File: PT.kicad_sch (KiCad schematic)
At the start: 4 parts

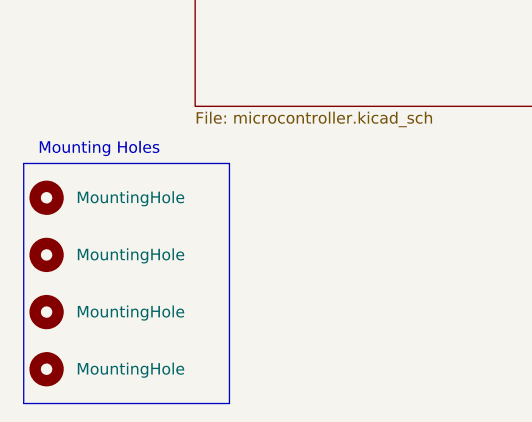
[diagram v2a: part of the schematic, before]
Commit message: Swap to STM32H563RIV6, and add split +3.3V and +3.3VA
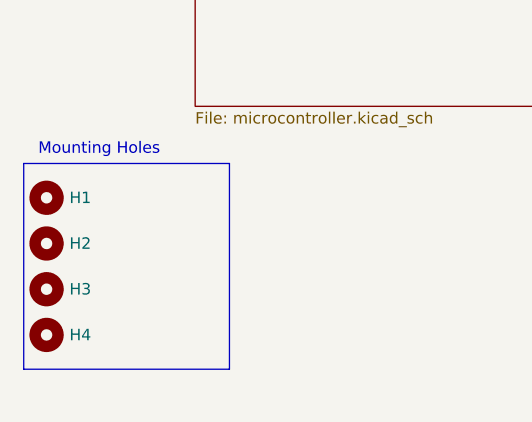
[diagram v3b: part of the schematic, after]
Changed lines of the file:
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@@
 	(rectangle
 		(start 20.32 172.72)
-		(end 43.18 199.39)
+		(end 43.18 195.58)
 		(stroke
 			(width 0)
@@
 	(symbol
 		(lib_id "Mechanical:MountingHole")
-		(at 22.86 189.23 0)
+		(at 22.86 176.53 0)
 		(unit 1)
 		(body_style 1)
@@
 		(in_pos_files yes)
 		(dnp no)
-		(property "Reference" "H3"
-			(at 25.4 187.9599 0)
-			(hide yes)
+		(property "Reference" "H1"
+			(at 25.4 176.53 0)
 			(show_name no)
 			(do_not_autoplace no)
@@
 		)
 		(property "Value" "MountingHole"
-			(at 26.162 189.23 0)
+			(at 26.162 176.53 0)
+			(hide yes)
 			(show_name no)
 			(do_not_autoplace no)
@@
 		)
 		(property "Footprint" "MountingHole:MountingHole_3.2mm_M3"
-			(at 22.86 189.23 0)
+			(at 22.86 176.53 0)
 			(hide yes)
 			(show_name no)
@@
 		)
 		(property "Datasheet" ""
-			(at 22.86 189.23 0)
+			(at 22.86 176.53 0)
 			(hide yes)
 			(show_name no)
@@
 		)
 		(property "Description" "Mounting Hole without connection"
-			(at 22.86 189.23 0)
+			(at 22.86 176.53 0)
 			(hide yes)
 			(show_name no)
@@
 			(project "PT"
 				(path "/0eb5ae8a-84ea-4b7e-bec4-bb4e0217d666"
-					(reference "H3")
+					(reference "H1")
 					(unit 1)
 				)
@@
 	(symbol
 		(lib_id "Mechanical:MountingHole")
-		(at 22.86 176.53 0)
+		(at 22.86 186.69 0)
 		(unit 1)
 		(body_style 1)
@@
 		(in_pos_files yes)
 		(dnp no)
-		(property "Reference" "H1"
-			(at 25.4 175.2599 0)
-			(hide yes)
+		(property "Reference" "H3"
+			(at 25.4 186.69 0)
 			(show_name no)
 			(do_not_autoplace no)
@@
 		)
 		(property "Value" "MountingHole"
-			(at 26.162 176.53 0)
+			(at 26.162 186.69 0)
+			(hide yes)
 			(show_name no)
 			(do_not_autoplace no)
@@
 		)
 		(property "Footprint" "MountingHole:MountingHole_3.2mm_M3"
-			(at 22.86 176.53 0)
+			(at 22.86 186.69 0)
 			(hide yes)
 			(show_name no)
@@
 		)
 		(property "Datasheet" ""
-			(at 22.86 176.53 0)
+			(at 22.86 186.69 0)
 			(hide yes)
 			(show_name no)
@@
 		)
 		(property "Description" "Mounting Hole without connection"
-			(at 22.86 176.53 0)
+			(at 22.86 186.69 0)
 			(hide yes)
 			(show_name no)
@@
 			(project "PT"
 				(path "/0eb5ae8a-84ea-4b7e-bec4-bb4e0217d666"
-					(reference "H1")
+					(reference "H3")
 					(unit 1)
 				)
@@
 	(symbol
 		(lib_id "Mechanical:MountingHole")
-		(at 22.86 182.88 0)
+		(at 22.86 191.77 0)
 		(unit 1)
 		(body_style 1)
@@
 		(in_pos_files yes)
 		(dnp no)
-		(property "Reference" "H2"
-			(at 25.4 181.6099 0)
-			(hide yes)
+		(property "Reference" "H4"
+			(at 25.4 191.77 0)
 			(show_name no)
 			(do_not_autoplace no)
@@
 		)
 		(property "Value" "MountingHole"
-			(at 26.162 182.88 0)
+			(at 26.162 191.77 0)
+			(hide yes)
 			(show_name no)
 			(do_not_autoplace no)
@@
 		)
 		(property "Footprint" "MountingHole:MountingHole_3.2mm_M3"
-			(at 22.86 182.88 0)
+			(at 22.86 191.77 0)
 			(hide yes)
 			(show_name no)
@@
 		)
 		(property "Datasheet" ""
-			(at 22.86 182.88 0)
+			(at 22.86 191.77 0)
 			(hide yes)
 			(show_name no)
@@
 		)
 		(property "Description" "Mounting Hole without connection"
-			(at 22.86 182.88 0)
+			(at 22.86 191.77 0)
 			(hide yes)
 			(show_name no)
@@
 			(project "PT"
 				(path "/0eb5ae8a-84ea-4b7e-bec4-bb4e0217d666"
-					(reference "H2")
+					(reference "H4")
 					(unit 1)
 				)
@@
 	(symbol
 		(lib_id "Mechanical:MountingHole")
-		(at 22.86 195.58 0)
+		(at 22.86 181.61 0)
 		(unit 1)
 		(body_style 1)
@@
 		(in_pos_files yes)
 		(dnp no)
-		(property "Reference" "H4"
-			(at 25.4 194.3099 0)
-			(hide yes)
+		(property "Reference" "H2"
+			(at 25.4 181.61 0)
 			(show_name no)
 			(do_not_autoplace no)
@@
 		)
 		(property "Value" "MountingHole"
-			(at 26.162 195.58 0)
+			(at 26.162 181.61 0)
+			(hide yes)
 			(show_name no)
 			(do_not_autoplace no)
@@
 		)
 		(property "Footprint" "MountingHole:MountingHole_3.2mm_M3"
-			(at 22.86 195.58 0)
+			(at 22.86 181.61 0)
 			(hide yes)
 			(show_name no)
@@
 		)
 		(property "Datasheet" ""
-			(at 22.86 195.58 0)
+			(at 22.86 181.61 0)
 			(hide yes)
 			(show_name no)
@@
 		)
 		(property "Description" "Mounting Hole without connection"
-			(at 22.86 195.58 0)
+			(at 22.86 181.61 0)
 			(hide yes)
 			(show_name no)
@@
 			(project "PT"
 				(path "/0eb5ae8a-84ea-4b7e-bec4-bb4e0217d666"
-					(reference "H4")
+					(reference "H2")
 					(unit 1)
 				)

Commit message: June 20th is not real and cant hurt me
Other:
- moved on the sheet: H1, H2, H3, H4
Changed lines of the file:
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@@
 	(symbol
 		(lib_id "Mechanical:MountingHole")
-		(at 22.86 176.53 0)
+		(at 25.4 176.53 0)
 		(unit 1)
 		(body_style 1)
@@
 		(dnp no)
 		(property "Reference" "H1"
+			(at 27.94 176.53 0)
+			(show_name no)
+			(do_not_autoplace no)
+			(effects
+				(font
+					(size 1.27 1.27)
+				)
+				(justify left)
+			)
+		)
+		(property "Value" "MountingHole"
+			(at 28.702 176.53 0)
+			(hide yes)
+			(show_name no)
+			(do_not_autoplace no)
+			(effects
+				(font
+					(size 1.27 1.27)
+				)
+				(justify left)
+			)
+		)
+		(property "Footprint" "MountingHole:MountingHole_3.2mm_M3"
 			(at 25.4 176.53 0)
-			(show_name no)
-			(do_not_autoplace no)
-			(effects
-				(font
-					(size 1.27 1.27)
-				)
-				(justify left)
-			)
-		)
-		(property "Value" "MountingHole"
-			(at 26.162 176.53 0)
-			(hide yes)
-			(show_name no)
-			(do_not_autoplace no)
-			(effects
-				(font
-					(size 1.27 1.27)
-				)
-				(justify left)
-			)
-		)
-		(property "Footprint" "MountingHole:MountingHole_3.2mm_M3"
-			(at 22.86 176.53 0)
-			(hide yes)
-			(show_name no)
-			(do_not_autoplace no)
-			(effects
-				(font
-					(size 1.27 1.27)
-				)
-			)
-		)
-		(property "Datasheet" ""
-			(at 22.86 176.53 0)
-			(hide yes)
-			(show_name no)
-			(do_not_autoplace no)
-			(effects
-				(font
-					(size 1.27 1.27)
-				)
-			)
-		)
-		(property "Description" "Mounting Hole without connection"
-			(at 22.86 176.53 0)
+			(hide yes)
+			(show_name no)
+			(do_not_autoplace no)
+			(effects
+				(font
+					(size 1.27 1.27)
+				)
+			)
+		)
+		(property "Datasheet" ""
+			(at 25.4 176.53 0)
+			(hide yes)
+			(show_name no)
+			(do_not_autoplace no)
+			(effects
+				(font
+					(size 1.27 1.27)
+				)
+			)
+		)
+		(property "Description" "Mounting Hole without connection"
+			(at 25.4 176.53 0)
 			(hide yes)
 			(show_name no)
@@
 	(symbol
 		(lib_id "Mechanical:MountingHole")
-		(at 22.86 186.69 0)
+		(at 25.4 186.69 0)
 		(unit 1)
 		(body_style 1)
@@
 		(dnp no)
 		(property "Reference" "H3"
+			(at 27.94 186.69 0)
+			(show_name no)
+			(do_not_autoplace no)
+			(effects
+				(font
+					(size 1.27 1.27)
+				)
+				(justify left)
+			)
+		)
+		(property "Value" "MountingHole"
+			(at 28.702 186.69 0)
+			(hide yes)
+			(show_name no)
+			(do_not_autoplace no)
+			(effects
+				(font
+					(size 1.27 1.27)
+				)
+				(justify left)
+			)
+		)
+		(property "Footprint" "MountingHole:MountingHole_3.2mm_M3"
 			(at 25.4 186.69 0)
-			(show_name no)
-			(do_not_autoplace no)
-			(effects
-				(font
-					(size 1.27 1.27)
-				)
-				(justify left)
-			)
-		)
-		(property "Value" "MountingHole"
-			(at 26.162 186.69 0)
-			(hide yes)
-			(show_name no)
-			(do_not_autoplace no)
-			(effects
-				(font
-					(size 1.27 1.27)
-				)
-				(justify left)
-			)
-		)
-		(property "Footprint" "MountingHole:MountingHole_3.2mm_M3"
-			(at 22.86 186.69 0)
-			(hide yes)
-			(show_name no)
-			(do_not_autoplace no)
-			(effects
-				(font
-					(size 1.27 1.27)
-				)
-			)
-		)
-		(property "Datasheet" ""
-			(at 22.86 186.69 0)
-			(hide yes)
-			(show_name no)
-			(do_not_autoplace no)
-			(effects
-				(font
-					(size 1.27 1.27)
-				)
-			)
-		)
-		(property "Description" "Mounting Hole without connection"
-			(at 22.86 186.69 0)
+			(hide yes)
+			(show_name no)
+			(do_not_autoplace no)
+			(effects
+				(font
+					(size 1.27 1.27)
+				)
+			)
+		)
+		(property "Datasheet" ""
+			(at 25.4 186.69 0)
+			(hide yes)
+			(show_name no)
+			(do_not_autoplace no)
+			(effects
+				(font
+					(size 1.27 1.27)
+				)
+			)
+		)
+		(property "Description" "Mounting Hole without connection"
+			(at 25.4 186.69 0)
 			(hide yes)
 			(show_name no)
@@
 	(symbol
 		(lib_id "Mechanical:MountingHole")
-		(at 22.86 191.77 0)
+		(at 25.4 191.77 0)
 		(unit 1)
 		(body_style 1)
@@
 		(dnp no)
 		(property "Reference" "H4"
+			(at 27.94 191.77 0)
+			(show_name no)
+			(do_not_autoplace no)
+			(effects
+				(font
+					(size 1.27 1.27)
+				)
+				(justify left)
+			)
+		)
+		(property "Value" "MountingHole"
+			(at 28.702 191.77 0)
+			(hide yes)
+			(show_name no)
+			(do_not_autoplace no)
+			(effects
+				(font
+					(size 1.27 1.27)
+				)
+				(justify left)
+			)
+		)
+		(property "Footprint" "MountingHole:MountingHole_3.2mm_M3"
 			(at 25.4 191.77 0)
-			(show_name no)
-			(do_not_autoplace no)
-			(effects
-				(font
-					(size 1.27 1.27)
-				)
-				(justify left)
-			)
-		)
-		(property "Value" "MountingHole"
-			(at 26.162 191.77 0)
-			(hide yes)
-			(show_name no)
-			(do_not_autoplace no)
-			(effects
-				(font
-					(size 1.27 1.27)
-				)
-				(justify left)
-			)
-		)
-		(property "Footprint" "MountingHole:MountingHole_3.2mm_M3"
-			(at 22.86 191.77 0)
-			(hide yes)
-			(show_name no)
-			(do_not_autoplace no)
-			(effects
-				(font
-					(size 1.27 1.27)
-				)
-			)
-		)
-		(property "Datasheet" ""
-			(at 22.86 191.77 0)
-			(hide yes)
-			(show_name no)
-			(do_not_autoplace no)
-			(effects
-				(font
-					(size 1.27 1.27)
-				)
-			)
-		)
-		(property "Description" "Mounting Hole without connection"
-			(at 22.86 191.77 0)
+			(hide yes)
+			(show_name no)
+			(do_not_autoplace no)
+			(effects
+				(font
+					(size 1.27 1.27)
+				)
+			)
+		)
+		(property "Datasheet" ""
+			(at 25.4 191.77 0)
+			(hide yes)
+			(show_name no)
+			(do_not_autoplace no)
+			(effects
+				(font
+					(size 1.27 1.27)
+				)
+			)
+		)
+		(property "Description" "Mounting Hole without connection"
+			(at 25.4 191.77 0)
 			(hide yes)
 			(show_name no)
@@
 	(symbol
 		(lib_id "Mechanical:MountingHole")
-		(at 22.86 181.61 0)
+		(at 25.4 181.61 0)
 		(unit 1)
 		(body_style 1)
@@
 		(dnp no)
 		(property "Reference" "H2"
+			(at 27.94 181.61 0)
+			(show_name no)
+			(do_not_autoplace no)
+			(effects
+				(font
+					(size 1.27 1.27)
+				)
+				(justify left)
+			)
+		)
+		(property "Value" "MountingHole"
+			(at 28.702 181.61 0)
+			(hide yes)
+			(show_name no)
+			(do_not_autoplace no)
+			(effects
+				(font
+					(size 1.27 1.27)
+				)
+				(justify left)
+			)
+		)
+		(property "Footprint" "MountingHole:MountingHole_3.2mm_M3"
 			(at 25.4 181.61 0)
-			(show_name no)
-			(do_not_autoplace no)
-			(effects
-				(font
-					(size 1.27 1.27)
-				)
-				(justify left)
-			)
-		)
-		(property "Value" "MountingHole"
-			(at 26.162 181.61 0)
-			(hide yes)
-			(show_name no)
-			(do_not_autoplace no)
-			(effects
-				(font
-					(size 1.27 1.27)
-				)
-				(justify left)
-			)
-		)
-		(property "Footprint" "MountingHole:MountingHole_3.2mm_M3"
-			(at 22.86 181.61 0)
-			(hide yes)
-			(show_name no)
-			(do_not_autoplace no)
-			(effects
-				(font
-					(size 1.27 1.27)
-				)
-			)
-		)
-		(property "Datasheet" ""
-			(at 22.86 181.61 0)
-			(hide yes)
-			(show_name no)
-			(do_not_autoplace no)
-			(effects
-				(font
-					(size 1.27 1.27)
-				)
-			)
-		)
-		(property "Description" "Mounting Hole without connection"
-			(at 22.86 181.61 0)
-			(hide yes)
-			(show_name no)
+			(hide yes)
+			(show_name no)
+			(do_not_autoplace no)
+			(effects
+				(font
+					(size 1.27 1.27)
+				)
+			)
+		)
+		(property "Datasheet" ""
+			(at 25.4 181.61 0)
+			(hide yes)
+			(show_name no)
+			(do_not_autoplace no)
+			(effects
+				(font
+					(size 1.27 1.27)
+				)
+			)
+		)
+		(property "Description" "Mounting Hole without connection"
+			(at 25.4 181.61 0)
+			(hide yes)
+			(show_name no)

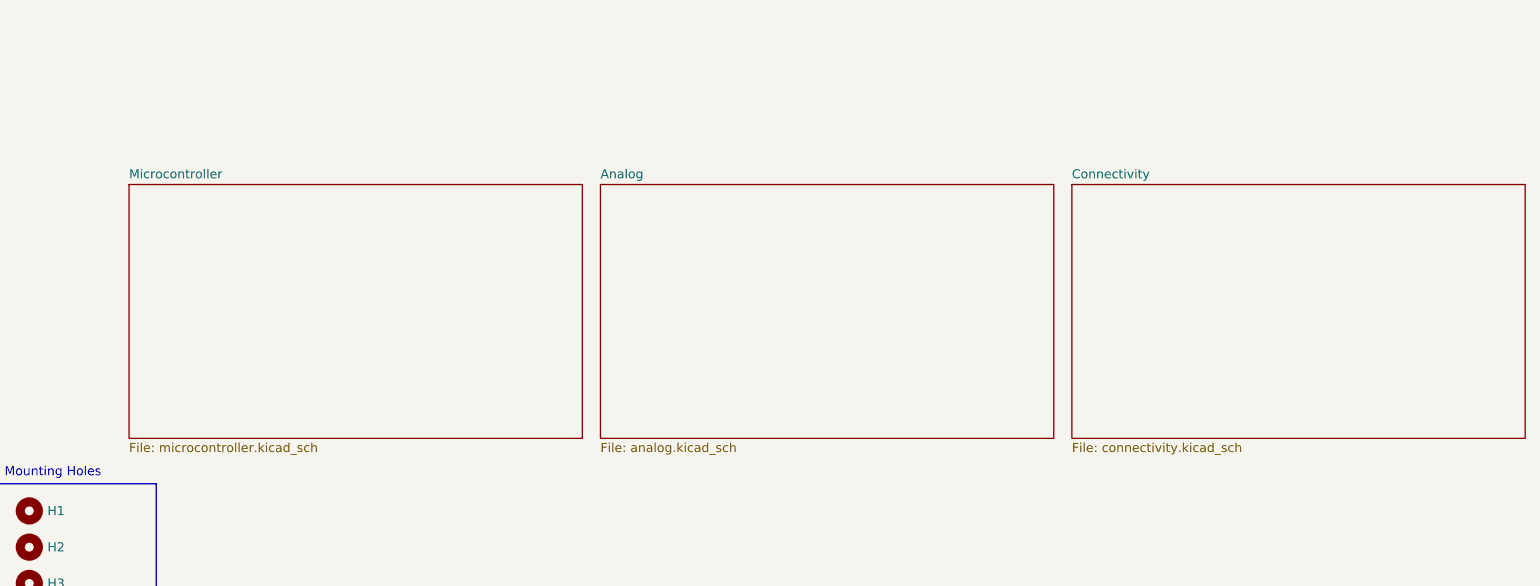
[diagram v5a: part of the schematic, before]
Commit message: Use sheet pins instead of global labels where appropriate
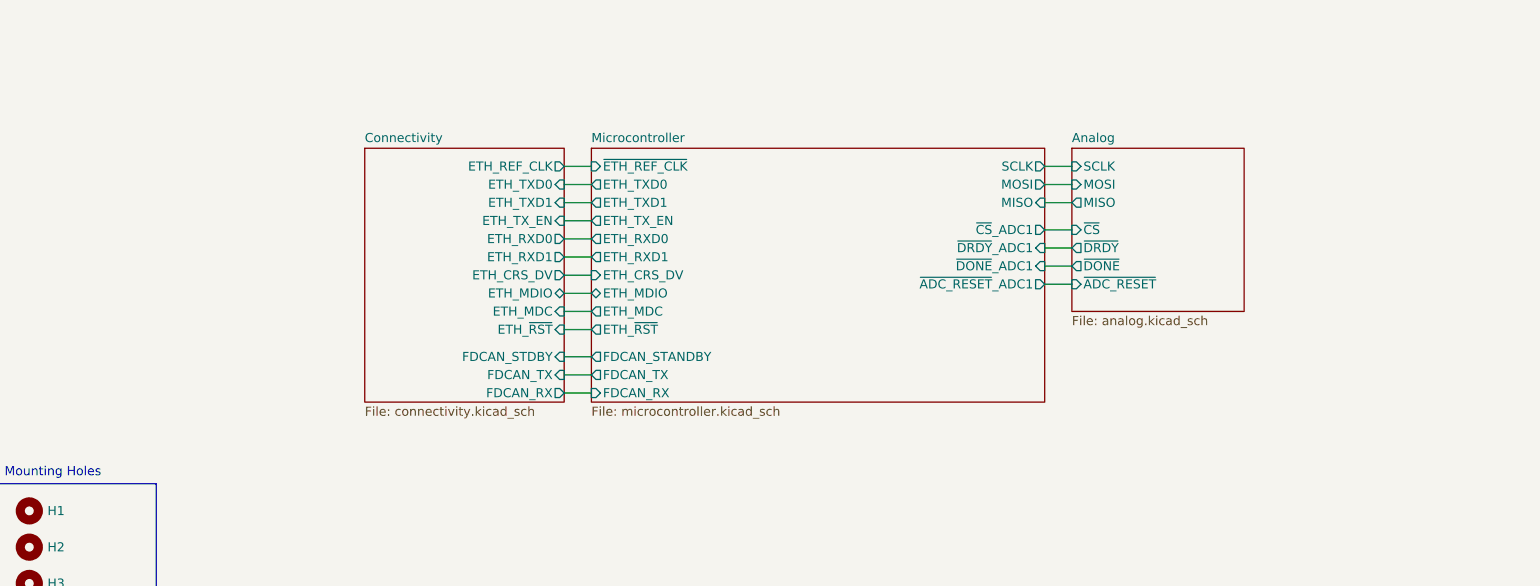
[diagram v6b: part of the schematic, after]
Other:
- sheet Analog ports: added MISO, MOSI, SCLK, ~{ADC_RESET}, ~{CS}, ~{DONE}, ~{DRDY}; removed none
- sheet Connectivity ports: added ETH_CRS_DV, ETH_MDC, ETH_MDIO, ETH_REF_CLK, ETH_RXD0, ETH_RXD1, ETH_TXD0, ETH_TXD1, ETH_TX_EN, ETH_~{RST}, FDCAN_RX, FDCAN_STDBY, FDCAN_TX; removed none
- sheet Microcontroller ports: added ETH_CRS_DV, ETH_MDC, ETH_MDIO, ETH_RXD0, ETH_RXD1, ETH_TXD0, ETH_TXD1, ETH_TX_EN, ETH_~{RST}, FDCAN_RX, FDCAN_STANDBY, FDCAN_TX, MISO, MOSI, SCLK, ~{ADC_RESET}_ADC1, ~{CS}_ADC1, ~{DONE}_ADC1, ~{DRDY}_ADC1, ~{ETH_REF_CLK}; removed none

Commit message: holy hell 2 adcs
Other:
- sheet Analog renamed ADC 1
- added sheet ADC 2 (analog.kicad_sch)
- sheet Microcontroller ports: added ~{ADC_RESET}_ADC2, ~{CS}_ADC2, ~{DONE}_ADC2, ~{DRDY}_ADC2; removed none
